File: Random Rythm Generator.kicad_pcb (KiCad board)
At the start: 2 copper layers, 72.4 x 53.3 mm, 29 parts, among them SW1 Randomise, U1 LM78L05_TO92, U2 40106, U3 4040, U4 74LS165

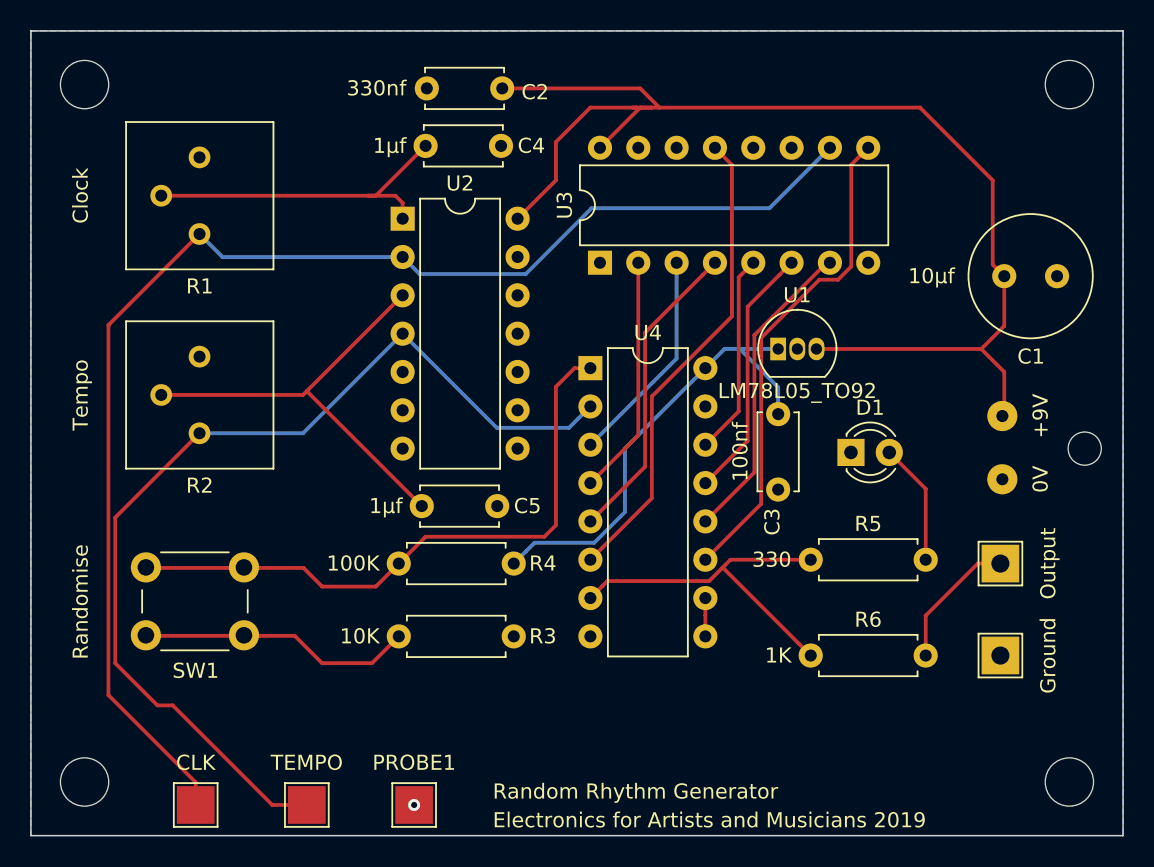
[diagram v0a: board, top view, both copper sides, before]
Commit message: add output pins
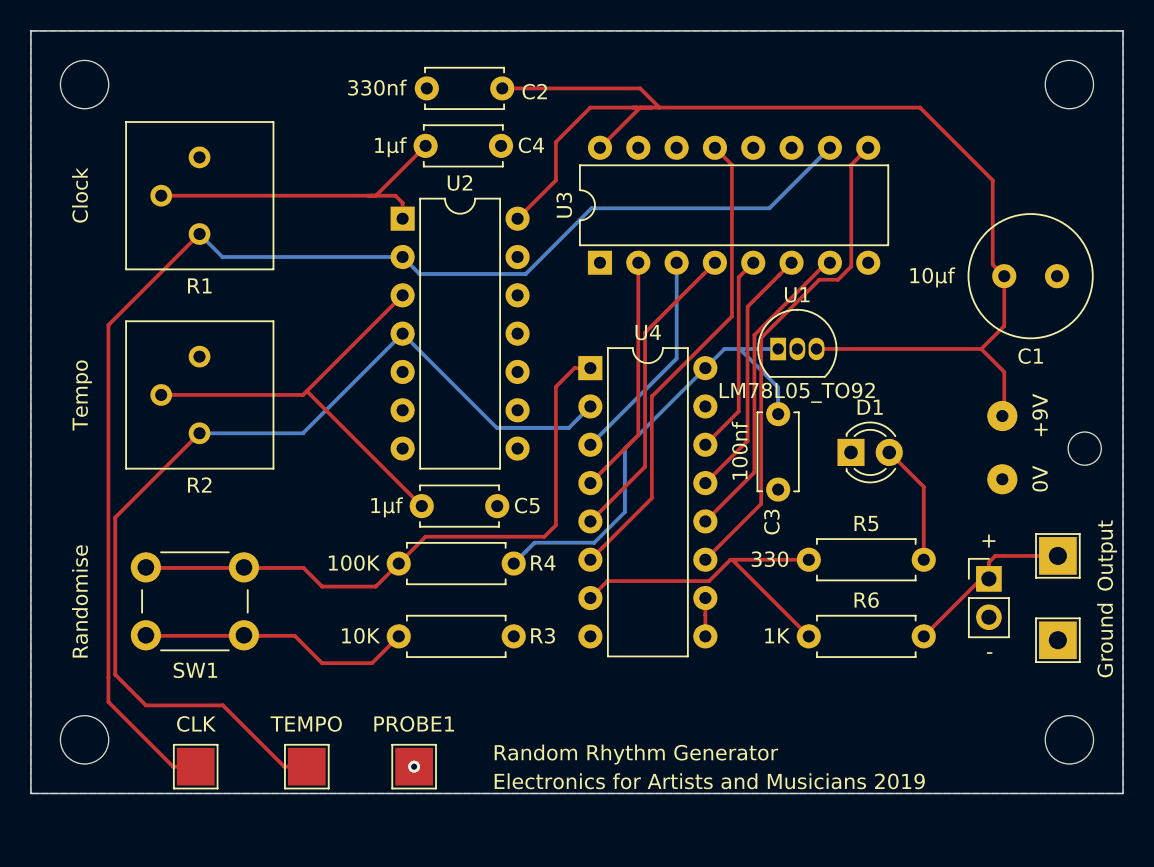
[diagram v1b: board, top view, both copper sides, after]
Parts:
- added +: +/-, Connector_PinHeader_2.54mm:PinHeader_1x02_P2.54mm_Vertical, F.Cu at (148.3, 82.5)
- moved Output2 3.94 mm to (152.9, 86.6)
- moved Output1 3.84 mm to (152.9, 81.0)
- moved REF** 2.79 mm to (153.7, 93.2)
- moved REF** 2.79 mm to (88.4, 93.2)
- moved PROBE1 2.54 mm to (110.2, 95.0)
- moved PROBE2 2.54 mm to (95.8, 95.0)
- moved PROBE3 2.54 mm to (103.1, 95.0)
- moved R6 1.28 mm to (136.4, 86.4)
- moved R5 0.13 mm to (136.4, 81.3)
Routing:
- net Net-(Output1-Pad1): track 9.39 -> 11.7 mm
- net Net-(PROBE2-Pad1): track 89.1 -> 87.4 mm
- net Net-(R5-Pad1): track 23.9 -> 22.7 mm
- net Net-(PROBE3-Pad1): track 66.0 -> 65.4 mm
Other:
- board size 72.4 x 53.3 mm -> 72.4 x 50.5 mm

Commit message: fix chip power supply by swapping vdd and vss
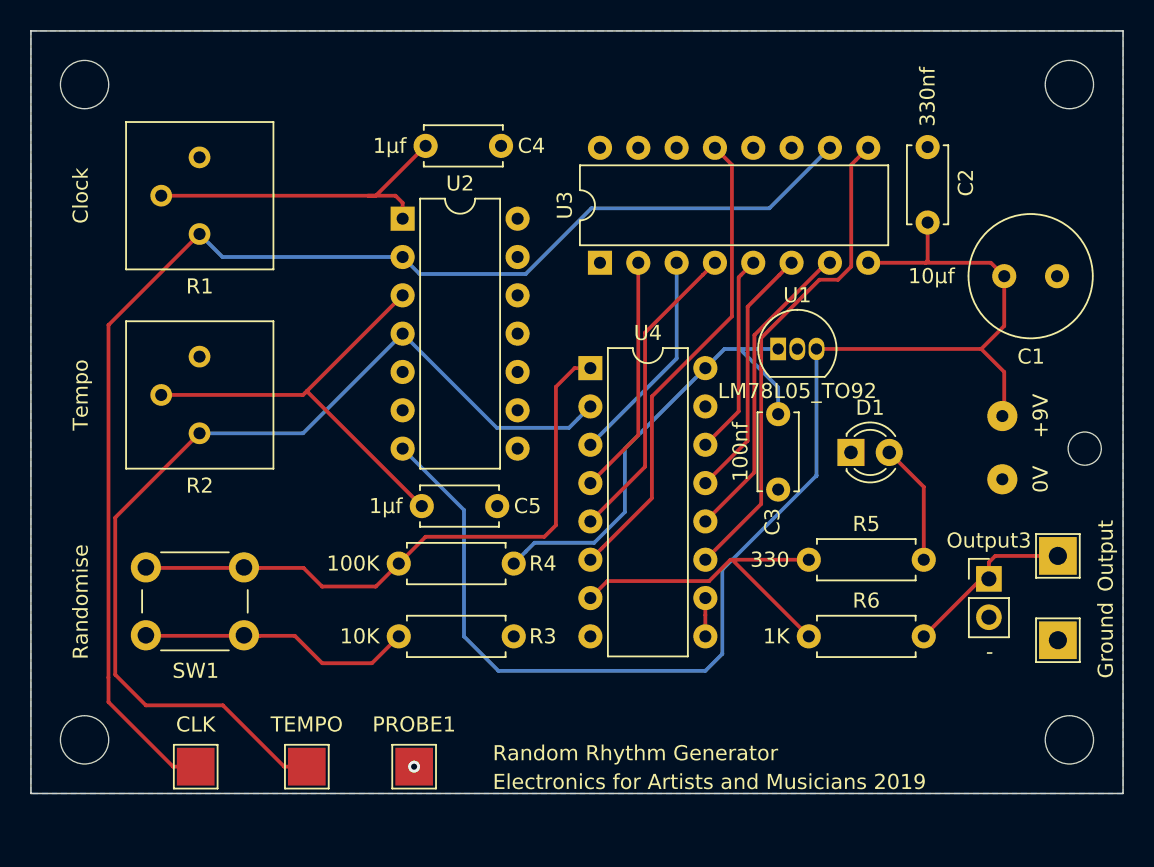
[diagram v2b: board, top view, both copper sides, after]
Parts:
- moved C2 29.6 mm to (144.3, 58.9), turned to 90 degrees
- renumbered + to Output3
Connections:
- U2 pad 14: +9V -> GND
- U2 pad 7: GND -> +9V
- U3 pad 16: +9V -> GND
- U3 pad 8: GND -> +9V
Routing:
- net +9V: track 81.9 -> 89.1 mm
